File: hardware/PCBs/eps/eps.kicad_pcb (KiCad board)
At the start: 4 copper layers, 59 parts, among them IC1 BQ29732DSER, IC2 BQ25302RTER, IC3 XCL240B333FR-G, IC4 TCPP01-M12, IC5 FUSB302BMPX, J1 UJC-H-G-SMT-2-P6-TR, J7 PH1-08-UA, J8 PRT-09279, Q1 CSD16406Q3, Q2 CSD16406Q3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

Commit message: Draft of EPS PCB half-way done
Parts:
- moved D4 97.4 mm to (43.0, 94.5), turned to 180 degrees
- moved R10 94.2 mm to (40.0, 91.0)
- moved Q4 93.0 mm to (48.5, 87.0), turned to -90 degrees
- moved R11 89.3 mm to (45.0, 91.0)
- moved J1 89.0 mm to (29.9, 92.3), turned to -90 degrees
- moved C10 85.5 mm to (46.5, 95.0), turned to -90 degrees
- moved R17 84.1 mm to (53.0, 98.5)
- moved C11 83.1 mm to (49.0, 96.0), turned to -90 degrees
- moved C9 83.0 mm to (49.0, 93.0), turned to -90 degrees
- moved IC2 82.0 mm to (60.0, 84.8)
- moved L1 77.2 mm to (195.4, 108.2)
- moved Q3 77.2 mm to (176.6, 117.8)
- moved BAT1 77.2 mm to (217.6, 51.5)
- moved BAT2 77.2 mm to (217.6, 75.7)
- moved C1 77.2 mm to (208.2, 108.2)
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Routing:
- net Net-(D3-K): vias 0 -> 8
- net GND: vias 0 -> 9
- net +3V3: vias 0 -> 2

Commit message: EPS pcb layout v0.1
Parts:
- moved IC3 164.6 mm to (68.2, 46.0), turned to 90 degrees
- moved R5 154.3 mm to (57.0, 75.5)
- moved D1 148.8 mm to (60.9, 77.5)
- moved R7 145.1 mm to (72.5, 71.0)
- moved R6 144.2 mm to (72.0, 73.5)
- moved R8 142.8 mm to (76.5, 69.0)
- moved R9 142.3 mm to (76.5, 73.5), turned to 180 degrees
- moved D2 141.3 mm to (73.0, 77.9), turned to -90 degrees
- moved L1 137.8 mm to (66.2, 60.5)
- moved C7 137.6 mm to (64.5, 45.5), turned to -90 degrees
- moved R1 136.0 mm to (74.3, 57.5)
- moved IC1 133.6 mm to (89.6, 52.5)
- moved C8 131.8 mm to (72.5, 46.0), turned to -90 degrees
- moved S1 128.7 mm to (41.1, 62.0), turned to 90 degrees
- moved Q3 128.1 mm to (57.6, 70.5), turned to 90 degrees
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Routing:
- net Net-(IC2-PMID): vias 0 -> 1
- net +3V3: vias 2 -> 4

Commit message: PCB-EPS 1/2
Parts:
- added FID1: Fiducial, Fiducial:Fiducial_1mm_Mask2mm, F.Cu at (104.0, 50.0)
- added FID2: Fiducial, Fiducial:Fiducial_1mm_Mask2mm, F.Cu at (180.5, 57.0)
- added FID3: Fiducial, Fiducial:Fiducial_1mm_Mask2mm, F.Cu at (95.5, 120.0)
- added H1: MountingHole_Pad, MountingHole:MountingHole_3.2mm_M3_Pad, F.Cu at (95.5, 50.0)
- added H2: MountingHole_Pad, MountingHole:MountingHole_3.2mm_M3_Pad, F.Cu at (180.6, 50.0)
- added H3: MountingHole_Pad, MountingHole:MountingHole_3.2mm_M3_Pad, F.Cu at (180.6, 129.1)
- added H4: MountingHole_Pad, MountingHole:MountingHole_3.2mm_M3_Pad, F.Cu at (95.5, 129.1)
- BAT1, BAT2, J7, NTC1, NTC2: moved to B.Cu
- moved BAT1 84.1 mm to (133.5, 53.3), turned to 90 degrees
- moved R1 74.4 mm to (147.8, 69.2)
- moved R22 73.3 mm to (149.7, 106.5), turned to 0 degrees
- moved R4 70.4 mm to (145.5, 72.2)
- moved C1 69.2 mm to (149.0, 72.2)
- moved R3 68.3 mm to (145.5, 75.2)
- moved C10 67.5 mm to (112.8, 107.8), turned to 90 degrees
- moved D4 67.3 mm to (109.0, 107.5), turned to 90 degrees
- moved NTC2 66.5 mm to (148.5, 97.2)
- moved C11 66.4 mm to (114.0, 109.8)
- moved C9 66.4 mm to (114.0, 106.8)
- moved IC4 66.2 mm to (116.8, 108.3)
- moved Q4 66.2 mm to (113.2, 100.8), turned to 90 degrees
- moved R21 66.2 mm to (140.0, 108.8), turned to 0 degrees
- moved J1 66.2 mm to (94.5, 106.5)
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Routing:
- net /BYPASS_CC2_PS: track 0.00 -> 50.2 mm
- net /VBUS: track 0.00 -> 42.1 mm
- net /USB_CC1: track 0.00 -> 41.5 mm, vias 0 -> 4
- net /BYPASS_CC1_PS: track 0.00 -> 40.7 mm
- net Net-(D3-K): track 0.00 -> 38.7 mm
- net /USB_SCL_PS: track 0.00 -> 29.7 mm, vias 0 -> 4
- net /USB_CC2: track 0.00 -> 28.5 mm
- net /INT_N_PS: track 0.00 -> 25.6 mm, vias 0 -> 4
- net /USB_SDA_PS: track 0.00 -> 24.7 mm, vias 0 -> 4
- net Net-(IC4-GATE): track 0.00 -> 22.9 mm
- net Net-(IC4-CC2C): track 0.00 -> 19.7 mm
- net Net-(IC4-CC1C): track 0.00 -> 18.7 mm
- net Net-(IC4-VBUS_CTRL): track 0.00 -> 14.9 mm
- net GND: track 0.00 -> 6.46 mm
- net +3V3: track 0.00 -> 5.12 mm, vias 4 -> 6
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- added copper zone on F.Cu, net +3V3
- added copper zone on In2.Cu, net +3V3
- added copper zone on F.Cu, net /VBUS
- added copper zone on In1.Cu, net GND
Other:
- board outline added: 96 x 90 mm

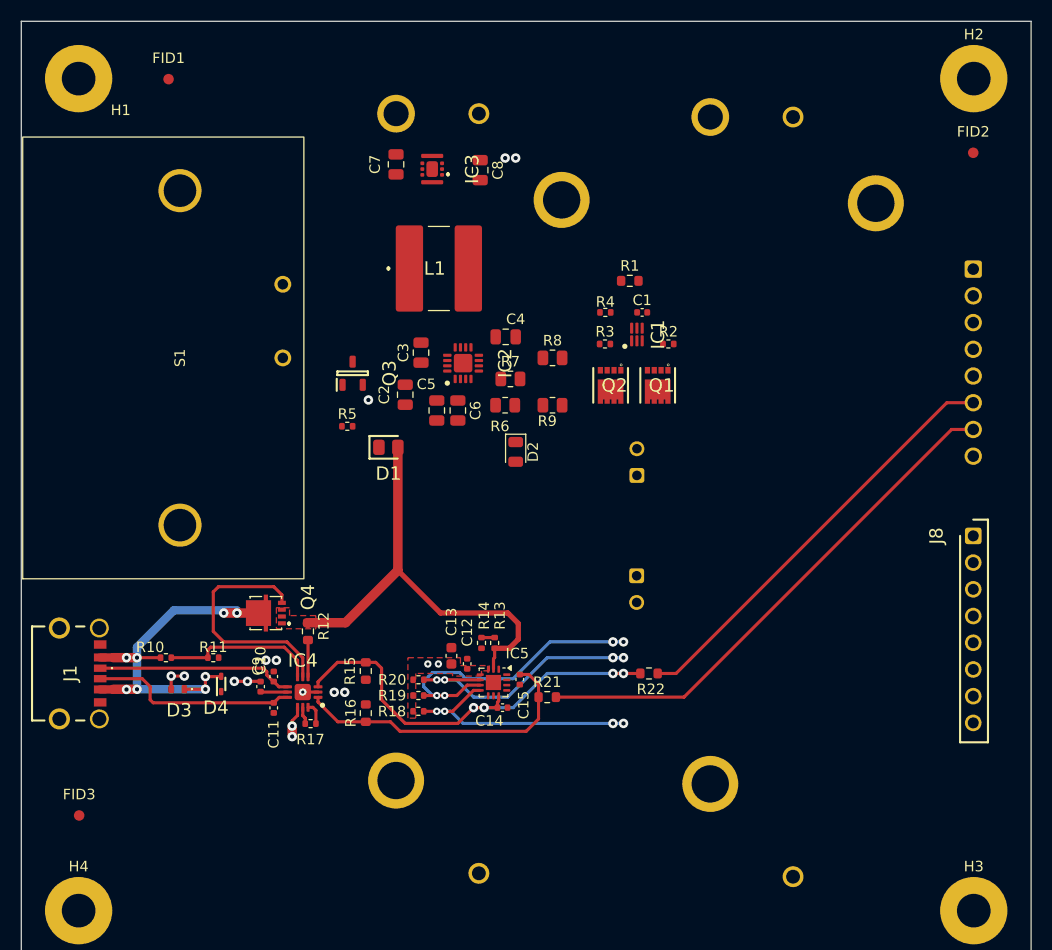
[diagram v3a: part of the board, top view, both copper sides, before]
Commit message: EPS-PCB gnd fill reamaining
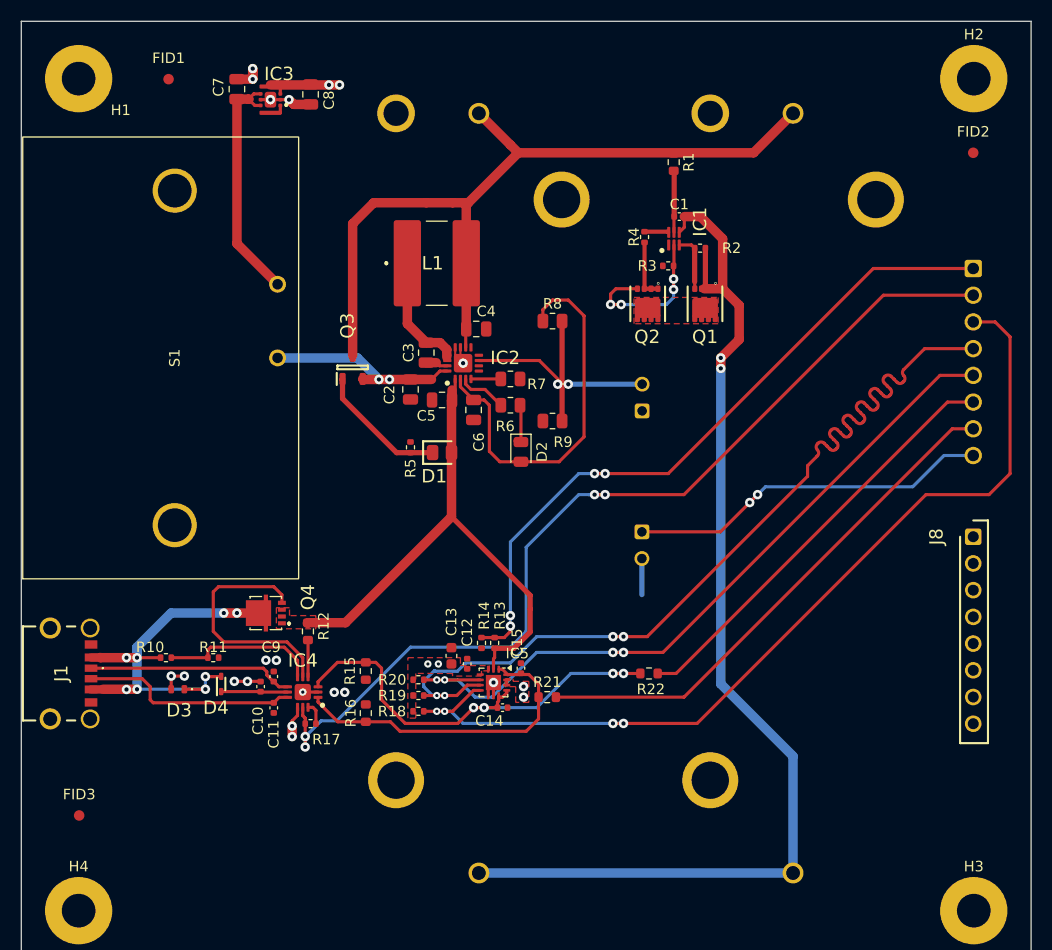
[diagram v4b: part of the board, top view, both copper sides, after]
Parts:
- moved C8 17.7 mm to (117.5, 51.5)
- moved IC3 16.7 mm to (114.0, 52.0)
- moved C7 16.7 mm to (110.5, 51.0), turned to 90 degrees
- moved R1 12.0 mm to (152.0, 57.9), turned to -90 degrees
- moved C1 9.77 mm to (152.6, 63.1)
- moved IC1 9.77 mm to (152.1, 65.2)
- moved R2 9.59 mm to (154.5, 66.1)
- moved R3 9.55 mm to (151.5, 67.8), turned to 180 degrees
- moved Q1 8.96 mm to (155.0, 71.4)
- moved Q2 8.51 mm to (149.6, 71.4)
- moved R4 8.08 mm to (149.2, 65.0), turned to -90 degrees
- moved R5 6.33 mm to (127.0, 85.0), turned to 90 degrees
- moved NTC1 6.16 mm to (149.0, 81.5)
- moved D1 5.12 mm to (130.0, 85.5)
- moved NTC2 4.20 mm to (149.0, 93.0)
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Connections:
- Q1 pad 9: (no net) -> Net-(Q1-D_1)
- Q2 pad 9: (no net) -> Net-(Q1-D_1)
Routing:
- net Net-(BAT1--): track 0.00 -> 106.3 mm, vias 0 -> 2
- net /FLT/_PS: track 1.65 -> 92.9 mm, vias 0 -> 4
- net Net-(BAT1-+): track 0.00 -> 77.9 mm
- net /ADC_VBUS_PS: track 1.25 -> 67.3 mm, vias 0 -> 4
- net /USB_SDA_PS: track 24.7 -> 89.3 mm
- net /USB_SCL_PS: track 29.7 -> 89.0 mm
- net /INT_N_PS: track 25.6 -> 71.0 mm
- net Net-(D2-A): track 0.00 -> 36.5 mm
- net /NTC_2_PS: track 0.00 -> 35.6 mm, vias 0 -> 2
- net Net-(IC2-TS): track 0.00 -> 27.5 mm, vias 0 -> 2
- net Net-(IC3-EN): track 0.00 -> 23.1 mm
- net GND: track 6.46 -> 26.8 mm, vias 9 -> 15
- net Net-(IC2-PMID): track 0.00 -> 18.4 mm, vias 1 -> 2
- net Net-(IC1-COUT): track 0.00 -> 16.2 mm, vias 0 -> 4
- net Net-(D1-K): track 0.00 -> 12.7 mm
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- added copper zone on F.Cu, net Net-(Q1-D_1)

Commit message: PCB - EPS done. RF started
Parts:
- added TP1: TestPoint, TestPoint:TestPoint_Plated_Hole_D2.0mm, F.Cu at (95.5, 116.8)
- added TP2: TestPoint, TestPoint:TestPoint_THTPad_2.0x2.0mm_Drill1.0mm, F.Cu at (101.0, 116.8)
- added TP3: TestPoint, TestPoint:TestPoint_Plated_Hole_D2.0mm, F.Cu at (119.2, 95.2)
- added TP4: TestPoint, TestPoint:TestPoint_Plated_Hole_D2.0mm, F.Cu at (148.2, 53.2)
- added TP5: TestPoint, TestPoint:TestPoint_Plated_Hole_D2.0mm, F.Cu at (115.8, 116.8)
- H1, H2, H3, H4: footprint MountingHole:MountingHole_3.2mm_M3_Pad -> MountingHole:MountingHole_3.2mm_M3_Pad_Via
- S1: moved to B.Cu
- moved FID3 11.5 mm to (102.2, 129.2)
- moved R11 2.25 mm to (110.5, 105.0)
- moved D4 1.80 mm to (110.0, 109.0), turned to 180 degrees
- moved R8 1.50 mm to (140.5, 74.5)
- moved D3 1.18 mm to (104.2, 109.0)
- moved R14 1.10 mm to (133.8, 102.5), turned to 90 degrees
- moved R15 0.75 mm to (122.0, 106.3)
- moved R16 0.75 mm to (122.0, 110.3)
- moved C10 0.50 mm to (112.8, 108.2), turned to 180 degrees
- moved R6 0.50 mm to (136.5, 81.5)
- turned S1 to -90 degrees
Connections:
- Q1 pad 9: Net-(Q1-D_1) -> (no net)
- Q2 pad 9: Net-(Q1-D_1) -> (no net)
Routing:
- net Net-(IC3-EN): track 23.1 -> 37.1 mm
- net +3V3: track 17.2 -> 7.26 mm
- net GND: track 26.8 -> 32.5 mm, vias 15 -> 226
- net /VBUS: track 52.2 -> 57.7 mm
- net /USB_CC1: track 42.6 -> 47.5 mm
- net Net-(BAT1-+): track 77.9 -> 81.3 mm
- net Net-(D3-K): track 41.4 -> 44.7 mm
- net /USB_SDA_PS: track 89.3 -> 92.7 mm
- net /USB_SCL_PS: track 89.0 -> 92.2 mm
- net Net-(IC2-SW_1): track 11.2 -> 9.00 mm
- net /ADC_VBUS_PS: track 67.3 -> 69.5 mm
- net Net-(IC1-COUT): track 16.2 -> 18.2 mm
- net /INT_N_PS: track 71.0 -> 72.7 mm
- net Net-(IC4-CC2C): track 20.6 -> 21.9 mm
- net /USB_CC2: track 30.8 -> 32.0 mm
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- added copper zone on B.Cu, net GND
- added copper zone on F.Cu, net GND
- added copper zone on F.Cu, net Net-(BAT1--)
- added copper zone on F.Cu, net Net-(IC2-PMID)
- added copper zone on F.Cu, net Net-(IC2-SW_1)
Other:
- board text added: "Jan Kusak"
- board text added: "{ "ViaStitching": "0.2", "gnd fill": { "HSpacing": "1", "VSpacing": "1", "Clearance": "0.6", "Randomize": false } }"

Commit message: RF finished
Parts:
- TP1: footprint TestPoint:TestPoint_Plated_Hole_D2.0mm -> TestPoint:TestPoint_THTPad_4.0x4.0mm_Drill2.0mm
- TP2: footprint TestPoint:TestPoint_THTPad_2.0x2.0mm_Drill1.0mm -> TestPoint:TestPoint_Plated_Hole_D2.0mm
- moved J8 17.8 mm to (180.5, 111.2), turned to 90 degrees
- moved FID1 13.7 mm to (95.5, 60.8)
- moved TP1 12.8 mm to (108.2, 116.8)
- moved FID3 10.9 mm to (95.5, 120.8)
- moved FID2 3.75 mm to (180.5, 60.8)
- moved C7 0.50 mm to (110.0, 51.0)
- moved C8 0.50 mm to (117.0, 51.5)
- moved IC3 0.50 mm to (113.5, 52.0)
- moved H3 0.07 mm to (180.5, 129.0)
- moved H2 0.07 mm to (180.5, 50.0)
- moved H4 0.07 mm to (95.5, 129.0)
- moved H1 0.07 mm to (95.5, 50.0)
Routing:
- net Net-(D3-K): track 44.7 -> 54.1 mm
- net Net-(IC3-EN): track 37.1 -> 36.5 mm
- net GND: vias 226 -> 177
- added copper zone on F.Cu, net Net-(IC3-EN)
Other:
- outline, holes or cut-outs redrawn
- board text added: "3.3 V"
- board text added: "5 V"
- board text added: "BAT"
- board text added: "GND"
- board text removed: "{ "ViaStitching": "0.2", "gnd fill": { "HSpacing": "1", "VSpacing": "1", "Clearance": "0.6", "Randomize": false } }"
